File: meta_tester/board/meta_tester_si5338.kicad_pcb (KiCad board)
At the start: 4 copper layers, 59 x 40 mm, 78 parts, among them J101 SMA_PCB, J102 SMA_PCB, J103 SMA_PCB, J104 SMA_PCB, J105 SMA_PCB, J106 SMA_PCB, J107 SMA_PCB, J108 SMA_PCB, P101 USB_OTG, U101 MAX5713/4/5-TSSOP14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

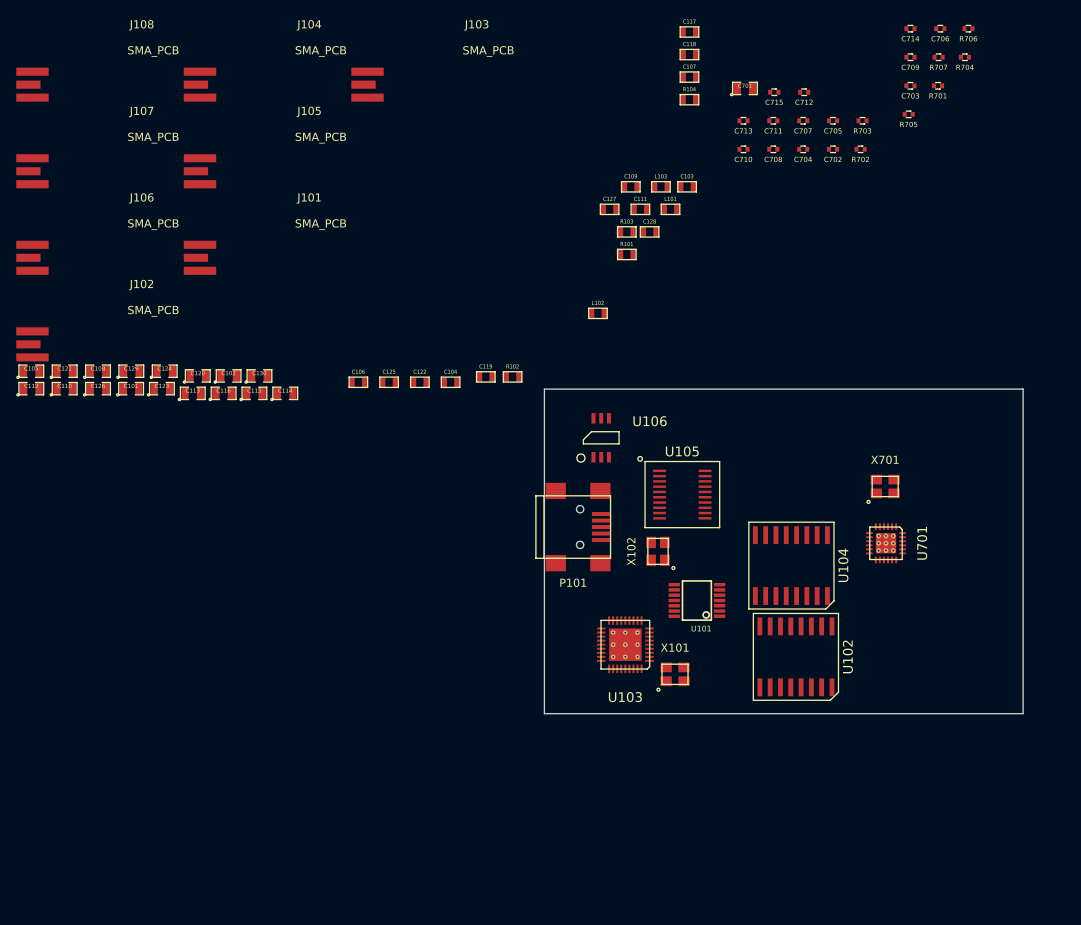
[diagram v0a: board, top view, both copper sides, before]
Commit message: reversed CTS/RTS
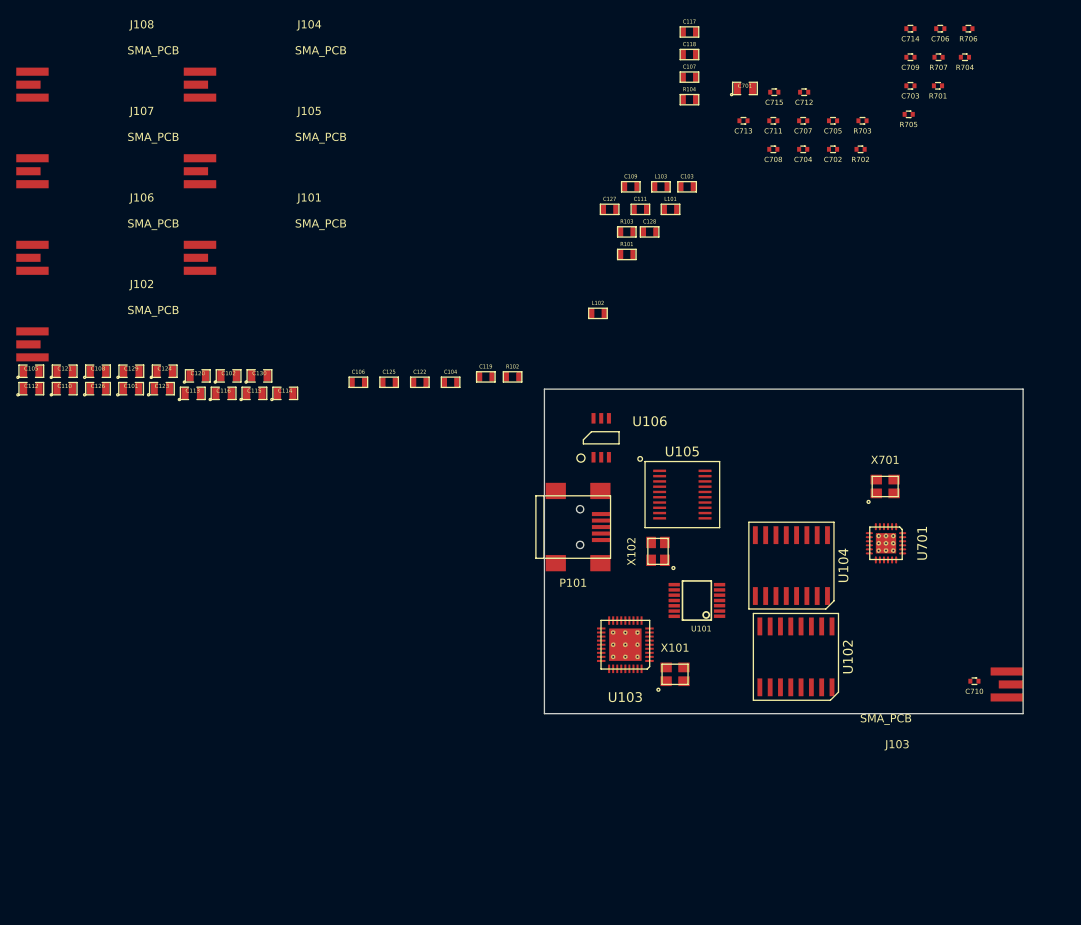
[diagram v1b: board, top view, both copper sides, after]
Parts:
- moved J103 108.8 mm to (196.5, 121.4), turned to 180 degrees
- moved C710 71.5 mm to (192.0, 121.0)
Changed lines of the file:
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@@
-(kicad_pcb (version 4) (host pcbnew 4.0.5)
+(kicad_pcb (version 4) (host pcbnew 4.0.2-stable)
   (general
     (links 225)
     (no_connects 207)
-    (area 138.924999 84.924999 198.075001 125.075001)
+    (area 73.64539 38.95 198.075001 125.075001)
     (thickness 1.6)
     (drawings 4)
@@
   )
   (module SM0402 (layer F.Cu)
-    (at 163.532857 55.445)
+    (at 192 121)
     (fp_text reference C710 (at 0 1.27) (layer F.SilkS)
       (effects (font (size 0.635 0.635) (thickness 0.15)))
@@
   )
   (module Connectors_RF:Border_Antenna (layer F.Cu)
-    (at 116.7 47.475)
-    (fp_text reference J103 (at 14 -7.4) (layer F.SilkS)
-      (effects (font (size 1 1) (thickness 0.15)))
-    )
-    (fp_text value SMA_PCB (at 15.4 -4.2) (layer F.SilkS)
-      (effects (font (size 1 1) (thickness 0.15)))
-    )
-    (pad 1 smd rect (at 0 0) (size 3 1) (layers F.Cu F.Paste F.Mask)
+    (at 196.5 121.4 180)
+    (fp_text reference J103 (at 14 -7.4 180) (layer F.SilkS)
+      (effects (font (size 1 1) (thickness 0.15)))
+    )
+    (fp_text value SMA_PCB (at 15.4 -4.2 180) (layer F.SilkS)
+      (effects (font (size 1 1) (thickness 0.15)))
+    )
+    (pad 1 smd rect (at 0 0 180) (size 3 1) (layers F.Cu F.Paste F.Mask)
       (net 25 /SI5338/CLK1_P))
-    (pad 2 smd rect (at 0.5 -1.6) (size 4 1) (layers F.Cu F.Paste F.Mask)
-      (net 1 GND))
-    (pad 2 smd rect (at 0.5 1.6) (size 4 1) (layers F.Cu F.Paste F.Mask)
-      (net 1 GND))
-  )
+    (pad 2 smd rect (at 0.5 -1.6 180) (size 4 1) (layers F.Cu F.Paste F.Mask)
+      (net 1 GND))
+    (pad 2 smd rect (at 0.5 1.6 180) (size 4 1) (layers F.Cu F.Paste F.Mask)
+      (net 1 GND))
+  )

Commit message: starting placing components
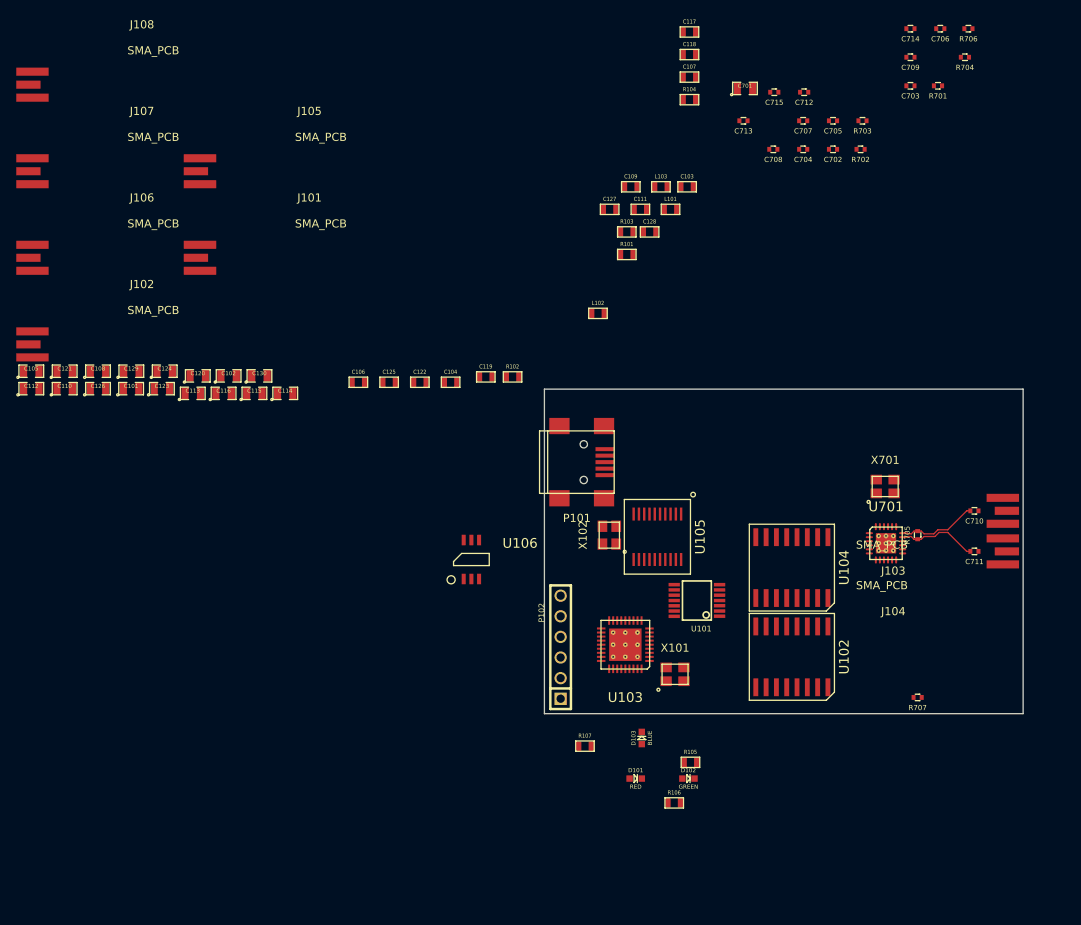
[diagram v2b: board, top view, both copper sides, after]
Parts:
- added D101: RED, General_SMD:LED-0603, F.Cu at (150.3, 133.0)
- added D102: GREEN, General_SMD:LED-0603, F.Cu at (156.7, 133.0)
- added D103: BLUE, General_SMD:LED-0603, F.Cu at (151.0, 128.0)
- added P102: CONN_01X06, Connectors_254mm:pin_array_6x1, F.Cu at (141.0, 116.8)
- added R105: RES_0603, General_SMD:SM0603, F.Cu at (157.0, 131.0)
- added R106: RES_0603, General_SMD:SM0603, F.Cu at (155.0, 136.0)
- added R107: RES_0603, General_SMD:SM0603, F.Cu at (144.0, 129.0)
- C101, C102, C105, C108, C110, C112, C113, C114, C115, C116, C120, C121, C123, C124, C126, C129, C130, C701: footprint SM0805 -> General_SMD:SM0805
- C103, C104, C106, C107, C109, C111, C117, C118, C119, C122, C125, C127, C128, L101, L102, L103, R101, R102, R103, R104: footprint SM0603 -> General_SMD:SM0603
- C702, C703, C704, C705, C706, C707, C708, C709, C710, C711, C712, C713, C714, C715, R701, R702, R703, R704, R705, R706, R707: footprint SM0402 -> General_SMD:SM0402
- moved J104 115.3 mm to (196.0, 105.0), turned to 180 degrees
- moved R707 78.9 mm to (185.0, 123.0)
- moved C711 58.6 mm to (192.0, 105.0)
- moved R705 51.9 mm to (185.0, 103.0), turned to 270 degrees
- moved U106 21.9 mm to (130.0, 106.0)
- moved J103 21.4 mm to (196.0, 100.0)
- moved C710 21.0 mm to (192.0, 100.0)
- moved P101 8.01 mm to (143.0, 94.0)
- moved X102 6.32 mm to (147.0, 103.0)
- moved U105 6.04 mm to (152.9, 103.2), turned to 180 degrees
- moved U102 0.50 mm to (169.5, 118.0)
- moved U104 0.26 mm to (169.5, 107.0)
- turned U701 to 0 degrees
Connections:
- U103 pad 25: Net-(U103-Pad25) -> /TMS
- U103 pad 28: Net-(U103-Pad28) -> /TCK
- U103 pad 29: Net-(U103-Pad29) -> /TDI
- U103 pad 30: Net-(U103-Pad30) -> /TDO
- U103 pad 6: Net-(U103-Pad6) -> +3V3
- U105 pad 11: /US1_CTS -> /US1_RTS
- U105 pad 16: /US1_RTS -> /US1_CTS
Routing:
- net /SI5338/clk1_1_N: track 0.00 -> 9.84 mm
- net /SI5338/clk1_1_P: track 0.00 -> 9.84 mm
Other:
- net class Default: clearance 0.2 -> 0.15; trace_width 0.25 -> 0.15; via_drill 0.4 -> 0.3
- rule trace_clearance: 0.2 -> 0.15
- rule trace_min: 0.2 -> 0.15

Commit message: working on pcb
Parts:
- moved U106 30.3 mm to (156.1, 90.6)
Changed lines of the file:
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@@
   (general
     (links 241)
-    (no_connects 222)
-    (area 138.924999 84.924999 198.075001 125.075001)
+    (no_connects 219)
+    (area 73.75 39.15 198.075001 136.848501)
     (thickness 1.6)
     (drawings 4)
@@
   )
   (module SOT:SOT-236-095mm (layer F.Cu)
-    (at 130 106)
+    (at 156.05 90.6)
     (fp_text reference U106 (at 6 -2 180) (layer F.SilkS)
       (effects (font (size 1.2 1.2) (thickness 0.15)))

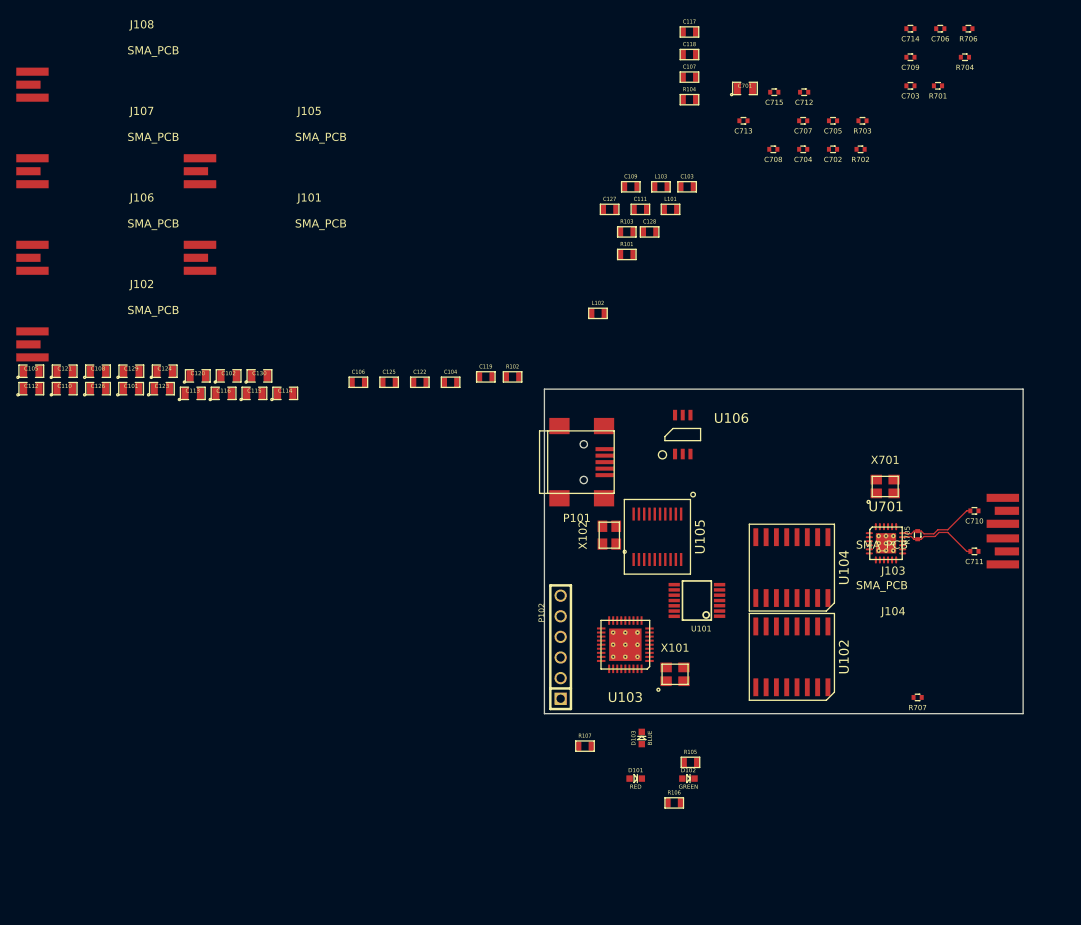
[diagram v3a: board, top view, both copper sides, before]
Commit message: starting simulation for sampling head + layout for clock board
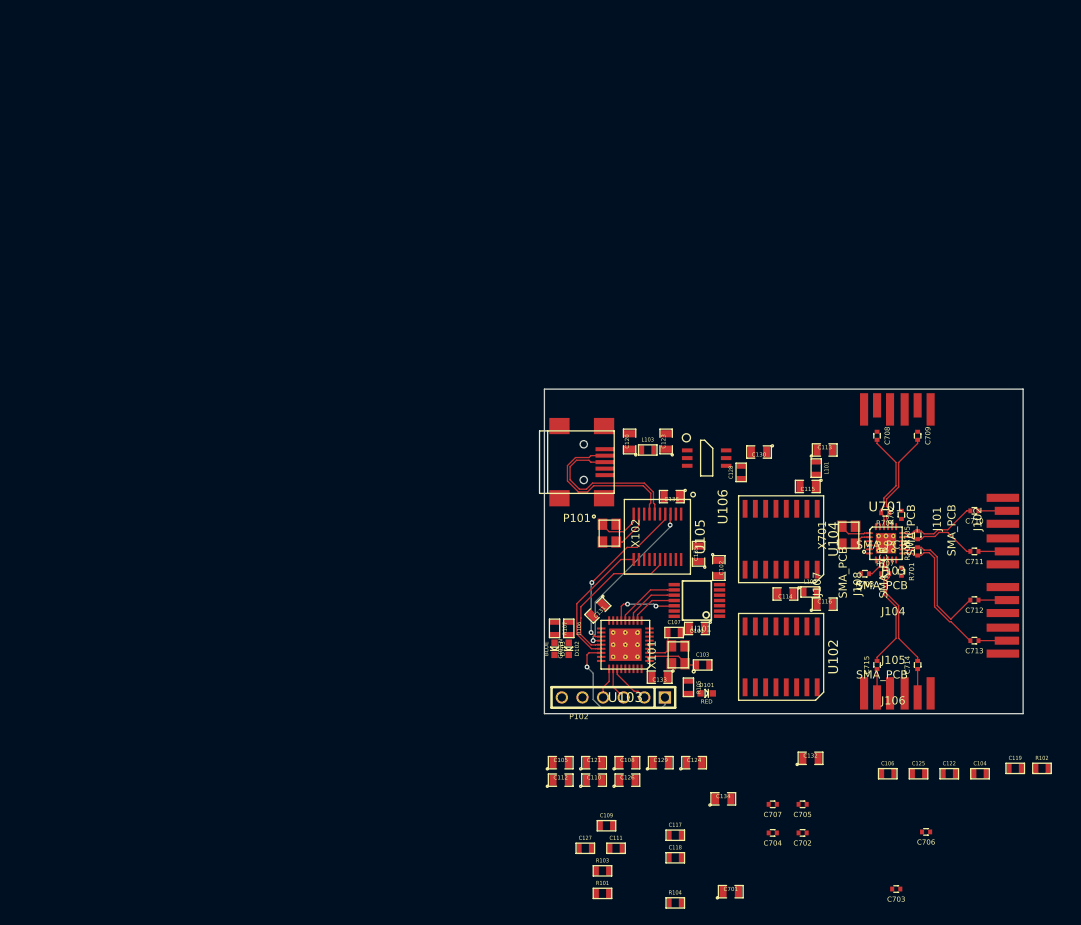
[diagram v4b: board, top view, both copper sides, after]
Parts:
- added C131: 100n, General_SMD:SM0805, F.Cu at (145.6, 112.2)
- added C132: 100n, General_SMD:SM0805, F.Cu at (171.8, 130.5)
- added C133: 100n, General_SMD:SM0805, F.Cu at (153.2, 120.5)
- added C134: 100n, General_SMD:SM0805, F.Cu at (161.0, 135.5)
- added C135: 100n, General_SMD:SM0805, F.Cu at (158.0, 105.3)
- added C136: 100n, General_SMD:SM0805, F.Cu at (154.7, 98.2)
- moved J108 133.1 mm to (185.0, 123.0), turned to 90 degrees
- moved J106 129.5 mm to (196.0, 116.0), turned to 180 degrees
- moved J107 123.1 mm to (180.0, 123.0), turned to 90 degrees
- moved J105 113.1 mm to (196.0, 111.0), turned to 180 degrees
- moved J102 109.9 mm to (185.0, 87.0), turned to 270 degrees
- moved C118 99.0 mm to (155.1, 142.8)
- moved R104 99.0 mm to (155.1, 148.3)
- moved C117 99.0 mm to (155.1, 140.0)
- moved C701 99.0 mm to (162.0, 146.9)
- moved C703 99.0 mm to (182.4, 146.6)
- moved C706 99.0 mm to (186.0, 139.6)
- moved J101 85.9 mm to (180.0, 87.0), turned to 270 degrees
- moved C705 84.3 mm to (170.8, 136.2)
- moved C707 84.3 mm to (167.1, 136.2)
- moved C702 84.3 mm to (170.8, 139.7)
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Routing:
- net /D_N: track 0.00 -> 21.2 mm
- net /D_P: track 0.00 -> 20.6 mm
- net /US1_TX: track 0.00 -> 20.6 mm, vias 0 -> 2
- net /US1_RX: track 0.00 -> 20.6 mm, vias 0 -> 2
- net /US1_CTS: track 0.00 -> 19.1 mm
- net /TMS: track 0.00 -> 18.0 mm, vias 0 -> 1
- net /US1_RTS: track 0.00 -> 16.8 mm
- net /SI5338/clk2_1_P: track 0.00 -> 16.7 mm
- net /SI5338/clk2_1_N: track 0.00 -> 16.7 mm
- net /SI5338/clk3_1_P: track 0.00 -> 14.4 mm
- net /SI5338/clk3_1_N: track 0.00 -> 14.4 mm
- net /SI5338/clk0_1_N: track 0.00 -> 12.6 mm
- net /SI5338/clk0_1_P: track 0.00 -> 12.6 mm
- net /CLR_DAC: track 0.00 -> 8.51 mm, vias 0 -> 2
- net /MOSI_DAC: track 0.00 -> 7.98 mm
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
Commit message: pcb'
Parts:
- moved R103 45.5 mm to (159.8, 101.0)
- moved R104 39.4 mm to (164.2, 110.0)
- moved C128 6.07 mm to (164.0, 89.2)
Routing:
- net /DAC3: track 0.00 -> 5.85 mm
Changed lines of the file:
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@@
   (general
     (links 253)
-    (no_connects 221)
-    (area 138.924999 84.924999 198.075001 125.075001)
+    (no_connects 190)
+    (area 137.974999 84.464286 201.683002 149.171251)
     (thickness 1.6)
     (drawings 4)
-    (tracks 252)
+    (tracks 256)
     (zones 0)
     (modules 91)
@@
   )
   (module General_SMD:SM0603 (layer F.Cu)
-    (at 163.25 95.262 90)
+    (at 164 89.238 90)
     (attr smd)
     (fp_text reference C128 (at 0 -1.27 90) (layer F.SilkS)
@@
     )
   )
-  (module General_SMD:SM0603 (layer F.Cu)
-    (at 146.156501 144.37275)
+  (module General_SMD:SM0603 locked (layer F.Cu)
+    (at 159.762 101)
     (attr smd)
     (fp_text reference R103 (at 0 -1.27) (layer F.SilkS)
@@
   )
   (module General_SMD:SM0603 (layer F.Cu)
-    (at 155.126501 148.32275)
+    (at 164.238 110)
     (attr smd)
     (fp_text reference R104 (at 0 -1.27) (layer F.SilkS)
@@
   (segment (start 153.9 117.5) (end 154.65 116.75) (width 0.15) (layer F.Cu) (net 6))
   (segment (start 154.65 116.75) (end 154.65 116.65) (width 0.15) (layer F.Cu) (net 6))
+  (segment (start 163.73 107.25) (end 163.73 109.746) (width 0.15) (layer F.Cu) (net 8))
+  (segment (start 163.73 109.746) (end 163.476 110) (width 0.15) (layer F.Cu) (net 8))
+  (segment (start 160.588 109.7488) (end 163.2248 109.7488) (width 0.15) (layer F.Cu) (net 8))
+  (segment (start 163.2248 109.7488) (end 163.476 110) (width 0.15) (layer F.Cu) (net 8))
   (segment (start 146.15 101.65) (end 146.15 101.75) (width 0.15) (layer F.Cu) (net 12))
   (segment (start 146.15 101.75) (end 146.975001 102.575001) (width 0.15) (layer F.Cu) (net 12))

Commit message: blabla
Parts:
- C110, C119, C121, C122, C124, C125, C126, C127, C129, C132, R101, R102, R103, R104: moved to B.Cu
- U106: footprint SOT:SOT-236-095mm -> SOT:SOT23-5
- moved C701 50.1 mm to (178.0, 99.5), turned to 90 degrees
- moved C127 50.0 mm to (181.0, 108.0), turned to 180 degrees
- moved C121 48.8 mm to (181.3, 98.2), turned to 180 degrees
- moved C126 44.9 mm to (185.7, 107.0)
- moved C111 42.3 mm to (161.2, 101.5), turned to 180 degrees
- moved C124 41.3 mm to (185.7, 100.9)
- moved C702 40.1 mm to (179.5, 100.5), turned to 90 degrees
- moved C117 39.8 mm to (144.0, 101.8), turned to 180 degrees
- moved C703 39.7 mm to (177.5, 107.2), turned to 270 degrees
- moved C707 39.5 mm to (184.0, 100.5), turned to 270 degrees
- moved C112 39.0 mm to (161.0, 99.8), turned to 180 degrees
- moved C118 38.4 mm to (145.8, 105.5), turned to 180 degrees
- moved R101 38.2 mm to (164.2, 113.5)
- moved R102 37.8 mm to (164.5, 119.8)
- moved C704 35.5 mm to (177.5, 105.8), turned to 180 degrees
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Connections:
- net Net-(C123-Pad1) renamed /5V01
- net Net-(C128-Pad2) renamed /L_N
- U101 pad 5: /DAC2 -> /DAC3
- U101 pad 6: /DAC3 -> /DAC2
- U104 pad 8: /DAC2 -> /DAC3
- U104 pad 9: /DAC3 -> /DAC2
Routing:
- net /VddO1: track 0.00 -> 11.3 mm
- net /VddO3: track 0.00 -> 10.9 mm
- net /VddO2: track 0.00 -> 9.62 mm
- net /VddO0: track 0.00 -> 9.62 mm
- net /DAC3: track 5.85 -> 0.03 mm
- net +3V3: track 0.00 -> 3.94 mm
- net /5V01: track 0.00 -> 3.75 mm
- net Net-(C118-Pad1): track 5.05 -> 7.25 mm
- net /L_N: track 0.00 -> 1.58 mm
- net Net-(C117-Pad1): track 5.75 -> 7.17 mm
- net /SDA: track 0.00 -> 1.22 mm
- net /SCL: track 0.00 -> 1.22 mm
- net Net-(D103-PadA): track 0.00 -> 1.00 mm
- net Net-(D102-PadA): track 0.00 -> 1.00 mm
- added copper zone on F.Cu, net +5V
- added copper zone on F.Cu, net /5V01
- added copper zone on F.Cu, net /PSU23
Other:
- net class POWER added: clearance 0.15, trace_width 0.25, via_dia 0.6, via_drill 0.3
- rule via_min_size: 0.4 -> 0.6

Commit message: working on layout
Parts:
- moved R104 6.55 mm to (164.5, 101.7)
- moved R103 3.25 mm to (164.3, 105.0)
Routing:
- added copper zone on F.Cu, net +3V3
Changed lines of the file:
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@@
   (general
     (links 253)
-    (no_connects 180)
-    (area 138.924999 84.924999 198.075001 125.075001)
+    (no_connects 170)
+    (area 137.974999 84.464286 198.075001 126.136)
     (thickness 1.6)
     (drawings 4)
@@
     (34 B.Paste user)
     (35 F.Paste user)
-    (36 B.SilkS user)
-    (37 F.SilkS user)
+    (36 B.SilkS user hide)
+    (37 F.SilkS user hide)
     (38 B.Mask user)
     (39 F.Mask user)
@@
     (pad_to_mask_clearance 0)
     (aux_axis_origin 0 0)
-    (visible_elements 7FFFFFFF)
+    (visible_elements 7FFFFF7F)
     (pcbplotparams
       (layerselection 0x00030_80000001)
@@
   )
   (module General_SMD:SM0603 locked (layer B.Cu)
-    (at 164.262 101.75)
+    (at 164.262 105)
     (attr smd)
     (fp_text reference R103 (at 0 1.27) (layer B.SilkS)
@@
   )
   (module General_SMD:SM0603 (layer B.Cu)
-    (at 164.238 108.25)
+    (at 164.462 101.7)
     (attr smd)
     (fp_text reference R104 (at 0 1.27) (layer B.SilkS)
@@
       )
     )
+  )
+  (zone (net 2) (net_name +3V3) (layer F.Cu) (hatch edge 0.508)
+    (connect_pads yes (clearance 0.15))
+    (min_thickness 0.15)
+    (fill yes (arc_segments 16) (thermal_gap 0.508) (thermal_bridge_width 0.508))
+    (polygon
+      (pts
+        (xy 159.7 92.9) (xy 161.2 92.9) (xy 161.6 93.3) (xy 163 93.3) (xy 163.2 93.1)
+        (xy 163.2 91.9) (xy 163 91.7) (xy 161.9 91.7) (xy 161.4 92.2) (xy 159.8 92.2)
+        (xy 159.6 92.4) (xy 159.6 92.8)
+      )
+    )
